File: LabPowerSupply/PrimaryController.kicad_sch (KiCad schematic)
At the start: 19 parts, among them Y1 8M

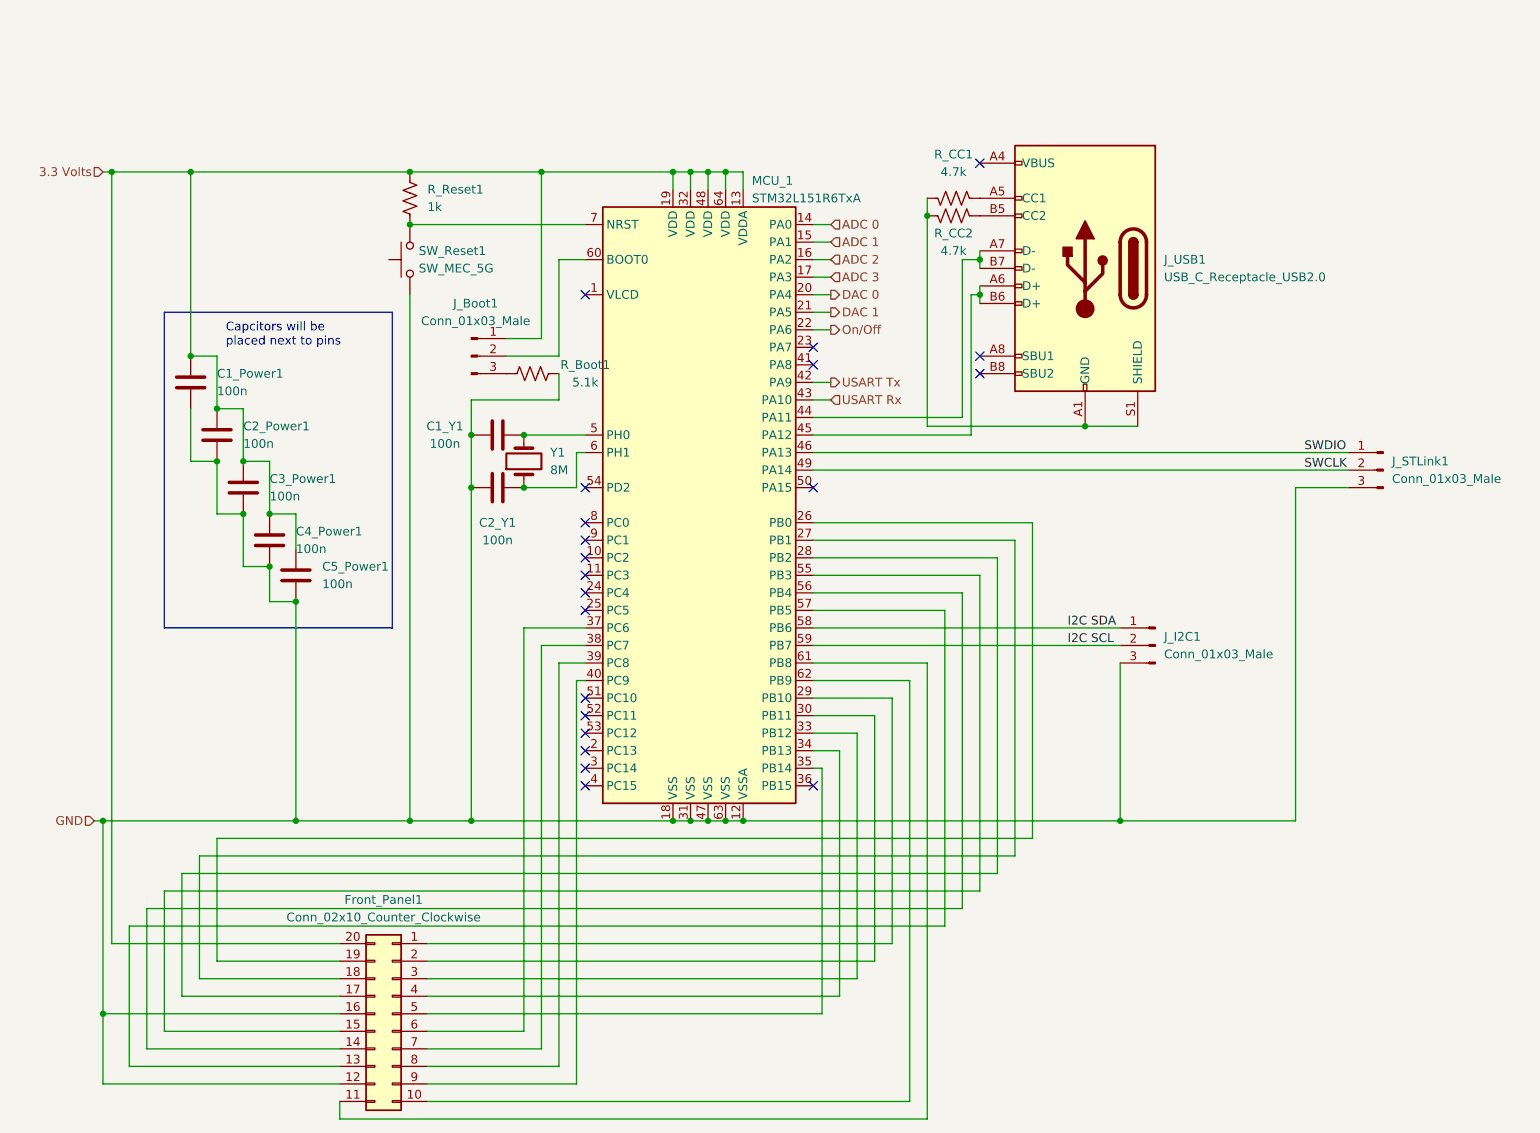
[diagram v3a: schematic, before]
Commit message: Resistor footprints changed to 0603
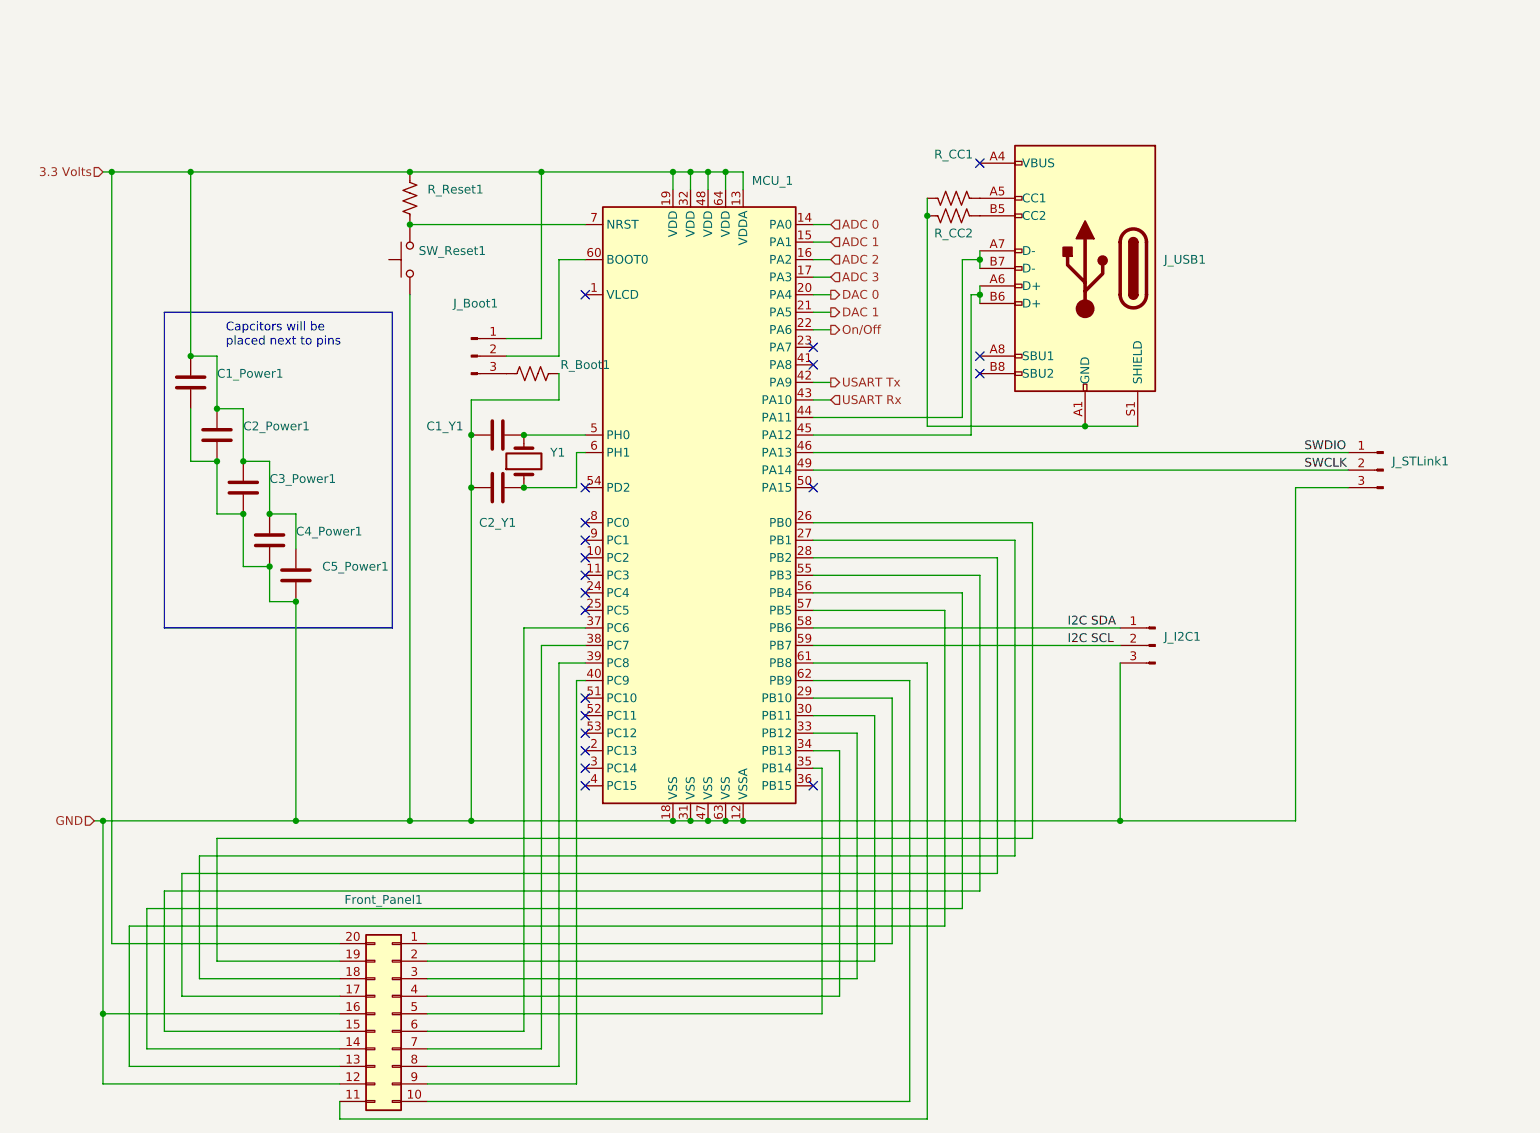
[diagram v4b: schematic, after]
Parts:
- C1_Power1, C1_Y1, C2_Power1, C2_Y1, C3_Power1, C4_Power1, C5_Power1: value 100n -> (none); footprint Capacitor_SMD:C_1210_3225Metric -> (none)
- Front_Panel1: value Conn_02x10_Counter_Clockwise -> (none); footprint Connector_IDC:IDC-Header_2x10_P2.54mm_Vertical -> (none)
- J_Boot1, J_I2C1, J_STLink1: value Conn_01x03_Male -> (none); footprint Connector_PinHeader_2.54mm:PinHeader_1x03_P2.54mm_Vertical -> (none)
- J_USB1: value USB_C_Receptacle_USB2.0 -> (none); footprint Connector_USB:USB_C_Receptacle_Palconn_UTC16-G -> (none)
- MCU_1: value STM32L151R6TxA -> (none); footprint Package_QFP:LQFP-64_10x10mm_P0.5mm -> (none)
- R_Boot1: value 5.1k -> (none); footprint Resistor_SMD:R_1210_3225Metric -> (none)
- R_CC1, R_CC2: value 4.7k -> (none); footprint Resistor_SMD:R_1210_3225Metric -> (none)
- R_Reset1: value 1k -> (none); footprint Resistor_SMD:R_1210_3225Metric -> (none)
- SW_Reset1: value SW_MEC_5G -> (none); footprint Button_Switch_SMD:SW_MEC_5GSH9 -> (none)
- Y1: value 8M -> (none); footprint Crystal:Crystal_HC18-U_Vertical -> (none)
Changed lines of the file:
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@@
       (effects (font (size 1.27 1.27)) (justify right))
     )
-    (property "Value" "8M" (id 1) (at 97.79 80.0099 90)
-      (effects (font (size 1.27 1.27)) (justify right))
-    )
-    (property "Footprint" "Crystal:Crystal_HC18-U_Vertical" (id 2) (at 93.98 78.74 0)
+    (property "Value" "" (id 1) (at 97.79 80.0099 90)
+      (effects (font (size 1.27 1.27)) (justify right))
+    )
+    (property "Footprint" "" (id 2) (at 93.98 78.74 0)
       (effects (font (size 1.27 1.27)) hide)
     )
@@
       (effects (font (size 1.27 1.27)) (justify right))
     )
-    (property "Value" "Conn_01x03_Male" (id 1) (at 219.71 81.2799 0)
-      (effects (font (size 1.27 1.27)) (justify right))
-    )
-    (property "Footprint" "Connector_PinHeader_2.54mm:PinHeader_1x03_P2.54mm_Vertical" (id 2) (at 218.44 80.01 0)
+    (property "Value" "" (id 1) (at 219.71 81.2799 0)
+      (effects (font (size 1.27 1.27)) (justify right))
+    )
+    (property "Footprint" "" (id 2) (at 218.44 80.01 0)
       (effects (font (size 1.27 1.27)) hide)
     )
@@
       (effects (font (size 1.27 1.27)) (justify right))
     )
-    (property "Value" "Conn_01x03_Male" (id 1) (at 186.69 106.6799 0)
-      (effects (font (size 1.27 1.27)) (justify right))
-    )
-    (property "Footprint" "Connector_PinHeader_2.54mm:PinHeader_1x03_P2.54mm_Vertical" (id 2) (at 185.42 105.41 0)
+    (property "Value" "" (id 1) (at 186.69 106.6799 0)
+      (effects (font (size 1.27 1.27)) (justify right))
+    )
+    (property "Footprint" "" (id 2) (at 185.42 105.41 0)
       (effects (font (size 1.27 1.27)) hide)
     )
@@
     (in_bom yes) (on_board yes)
     (property "Reference" "C2_Y1" (id 0) (at 90.17 87.63 90))
-    (property "Value" "100n" (id 1) (at 90.17 90.17 90))
-    (property "Footprint" "Capacitor_SMD:C_1210_3225Metric" (id 2) (at 93.98 83.5152 0)
+    (property "Value" "" (id 1) (at 90.17 90.17 90))
+    (property "Footprint" "" (id 2) (at 93.98 83.5152 0)
       (effects (font (size 1.27 1.27)) hide)
     )
@@
     (in_bom yes) (on_board yes)
     (property "Reference" "R_CC2" (id 0) (at 156.21 45.72 90))
-    (property "Value" "4.7k" (id 1) (at 156.21 48.26 90))
-    (property "Footprint" "Resistor_SMD:R_1210_3225Metric" (id 2) (at 155.956 42.164 90)
+    (property "Value" "" (id 1) (at 156.21 48.26 90))
+    (property "Footprint" "" (id 2) (at 155.956 42.164 90)
       (effects (font (size 1.27 1.27)) hide)
     )
@@
     (in_bom yes) (on_board yes) (fields_autoplaced)
     (property "Reference" "Front_Panel1" (id 0) (at 73.66 142.24 0))
-    (property "Value" "Conn_02x10_Counter_Clockwise" (id 1) (at 73.66 144.78 0))
-    (property "Footprint" "Connector_IDC:IDC-Header_2x10_P2.54mm_Vertical" (id 2) (at 74.93 158.75 0)
+    (property "Value" "" (id 1) (at 73.66 144.78 0))
+    (property "Footprint" "" (id 2) (at 74.93 158.75 0)
       (effects (font (size 1.27 1.27)) hide)
     )
@@
       (effects (font (size 1.27 1.27)) (justify left))
     )
-    (property "Value" "100n" (id 1) (at 60.96 91.4399 0)
-      (effects (font (size 1.27 1.27)) (justify left))
-    )
-    (property "Footprint" "Capacitor_SMD:C_1210_3225Metric" (id 2) (at 58.1152 93.98 0)
+    (property "Value" "" (id 1) (at 60.96 91.4399 0)
+      (effects (font (size 1.27 1.27)) (justify left))
+    )
+    (property "Footprint" "" (id 2) (at 58.1152 93.98 0)
       (effects (font (size 1.27 1.27)) hide)
     )
@@
       (effects (font (size 1.27 1.27)) (justify right))
     )
-    (property "Value" "SW_MEC_5G" (id 1) (at 78.74 50.7999 90)
-      (effects (font (size 1.27 1.27)) (justify right))
-    )
-    (property "Footprint" "Button_Switch_SMD:SW_MEC_5GSH9" (id 2) (at 72.39 49.53 0)
+    (property "Value" "" (id 1) (at 78.74 50.7999 90)
+      (effects (font (size 1.27 1.27)) (justify right))
+    )
+    (property "Footprint" "" (id 2) (at 72.39 49.53 0)
       (effects (font (size 1.27 1.27)) hide)
     )
@@
       (effects (font (size 1.27 1.27)) (justify left))
     )
-    (property "Value" "100n" (id 1) (at 64.77 96.5199 0)
-      (effects (font (size 1.27 1.27)) (justify left))
-    )
-    (property "Footprint" "Capacitor_SMD:C_1210_3225Metric" (id 2) (at 61.9252 99.06 0)
+    (property "Value" "" (id 1) (at 64.77 96.5199 0)
+      (effects (font (size 1.27 1.27)) (justify left))
+    )
+    (property "Footprint" "" (id 2) (at 61.9252 99.06 0)
       (effects (font (size 1.27 1.27)) hide)
     )
@@
     (in_bom yes) (on_board yes)
     (property "Reference" "C1_Y1" (id 0) (at 82.55 73.66 90))
-    (property "Value" "100n" (id 1) (at 82.55 76.2 90))
-    (property "Footprint" "Capacitor_SMD:C_1210_3225Metric" (id 2) (at 93.98 73.9648 0)
+    (property "Value" "" (id 1) (at 82.55 76.2 90))
+    (property "Footprint" "" (id 2) (at 93.98 73.9648 0)
       (effects (font (size 1.27 1.27)) hide)
     )
@@
       (effects (font (size 1.27 1.27)) (justify left))
     )
-    (property "Value" "1k" (id 1) (at 80.01 41.9099 0)
-      (effects (font (size 1.27 1.27)) (justify left))
-    )
-    (property "Footprint" "Resistor_SMD:R_1210_3225Metric" (id 2) (at 78.486 40.894 90)
+    (property "Value" "" (id 1) (at 80.01 41.9099 0)
+      (effects (font (size 1.27 1.27)) (justify left))
+    )
+    (property "Footprint" "" (id 2) (at 78.486 40.894 90)
       (effects (font (size 1.27 1.27)) hide)
     )
@@
     (in_bom yes) (on_board yes)
     (property "Reference" "R_CC1" (id 0) (at 156.21 34.29 90))
-    (property "Value" "4.7k" (id 1) (at 156.21 36.83 90))
-    (property "Footprint" "Resistor_SMD:R_1210_3225Metric" (id 2) (at 155.956 39.624 90)
+    (property "Value" "" (id 1) (at 156.21 36.83 90))
+    (property "Footprint" "" (id 2) (at 155.956 39.624 90)
       (effects (font (size 1.27 1.27)) hide)
     )
@@
     (in_bom yes) (on_board yes) (fields_autoplaced)
     (property "Reference" "J_Boot1" (id 0) (at 86.995 55.88 0))
-    (property "Value" "Conn_01x03_Male" (id 1) (at 86.995 58.42 0))
-    (property "Footprint" "Connector_PinHeader_2.54mm:PinHeader_1x03_P2.54mm_Vertical" (id 2) (at 86.36 63.5 0)
+    (property "Value" "" (id 1) (at 86.995 58.42 0))
+    (property "Footprint" "" (id 2) (at 86.36 63.5 0)
       (effects (font (size 1.27 1.27)) hide)
     )
@@
       (effects (font (size 1.27 1.27)) (justify left))
     )
-    (property "Value" "100n" (id 1) (at 53.34 76.1999 0)
-      (effects (font (size 1.27 1.27)) (justify left))
-    )
-    (property "Footprint" "Capacitor_SMD:C_1210_3225Metric" (id 2) (at 50.4952 78.74 0)
+    (property "Value" "" (id 1) (at 53.34 76.1999 0)
+      (effects (font (size 1.27 1.27)) (justify left))
+    )
+    (property "Footprint" "" (id 2) (at 50.4952 78.74 0)
       (effects (font (size 1.27 1.27)) hide)
     )
@@
       (effects (font (size 1.27 1.27)) (justify left))
     )
-    (property "Value" "100n" (id 1) (at 49.53 68.5799 0)
-      (effects (font (size 1.27 1.27)) (justify left))
-    )
-    (property "Footprint" "Capacitor_SMD:C_1210_3225Metric" (id 2) (at 46.6852 71.12 0)
+    (property "Value" "" (id 1) (at 49.53 68.5799 0)
+      (effects (font (size 1.27 1.27)) (justify left))
+    )
+    (property "Footprint" "" (id 2) (at 46.6852 71.12 0)
       (effects (font (size 1.27 1.27)) hide)
     )
@@
     (in_bom yes) (on_board yes)
     (property "Reference" "R_Boot1" (id 0) (at 102.87 64.77 90))
-    (property "Value" "5.1k" (id 1) (at 102.87 67.31 90))
-    (property "Footprint" "Resistor_SMD:R_1210_3225Metric" (id 2) (at 95.504 65.024 90)
+    (property "Value" "" (id 1) (at 102.87 67.31 90))
+    (property "Footprint" "" (id 2) (at 95.504 65.024 90)
       (effects (font (size 1.27 1.27)) hide)
     )
@@
       (effects (font (size 1.27 1.27)) (justify right))
     )
-    (property "Value" "USB_C_Receptacle_USB2.0" (id 1) (at 186.69 52.0699 0)
-      (effects (font (size 1.27 1.27)) (justify right))
-    )
-    (property "Footprint" "Connector_USB:USB_C_Receptacle_Palconn_UTC16-G" (id 2) (at 171.45 50.8 0)
+    (property "Value" "" (id 1) (at 186.69 52.0699 0)
+      (effects (font (size 1.27 1.27)) (justify right))
+    )
+    (property "Footprint" "" (id 2) (at 171.45 50.8 0)
       (effects (font (size 1.27 1.27)) hide)
     )
@@
       (effects (font (size 1.27 1.27)) (justify left))
     )
-    (property "Value" "STM32L151R6TxA" (id 1) (at 127 40.64 0)
-      (effects (font (size 1.27 1.27)) (justify left))
-    )
-    (property "Footprint" "Package_QFP:LQFP-64_10x10mm_P0.5mm" (id 2) (at 105.41 128.27 0)
+    (property "Value" "" (id 1) (at 127 40.64 0)
+      (effects (font (size 1.27 1.27)) (justify left))
+    )
+    (property "Footprint" "" (id 2) (at 105.41 128.27 0)
       (effects (font (size 1.27 1.27)) (justify right) hide)
     )
@@
       (effects (font (size 1.27 1.27)) (justify left))
     )
-    (property "Value" "100n" (id 1) (at 57.15 83.8199 0)
-      (effects (font (size 1.27 1.27)) (justify left))
-    )
-    (property "Footprint" "Capacitor_SMD:C_1210_3225Metric" (id 2) (at 54.3052 86.36 0)
-      (effects (font (size 1.27 1.27)) hide)
-    )
+    (property "Value" "" (id 1) (at 57.15 83.8199 0)
+      (effects (font (size 1.27 1.27)) (justify left))
+    )
+    (property "Footprint" "" (id 2) (at 54.3052 86.36 0)
+      (effects (font (size 1.27 1.27)) hide)
+    )
